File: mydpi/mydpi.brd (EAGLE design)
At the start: 40 x 20 mm, 33 parts, among them U1 MEGA32U4-MU, U2 AP7381-33Y-13, Y1 830069392

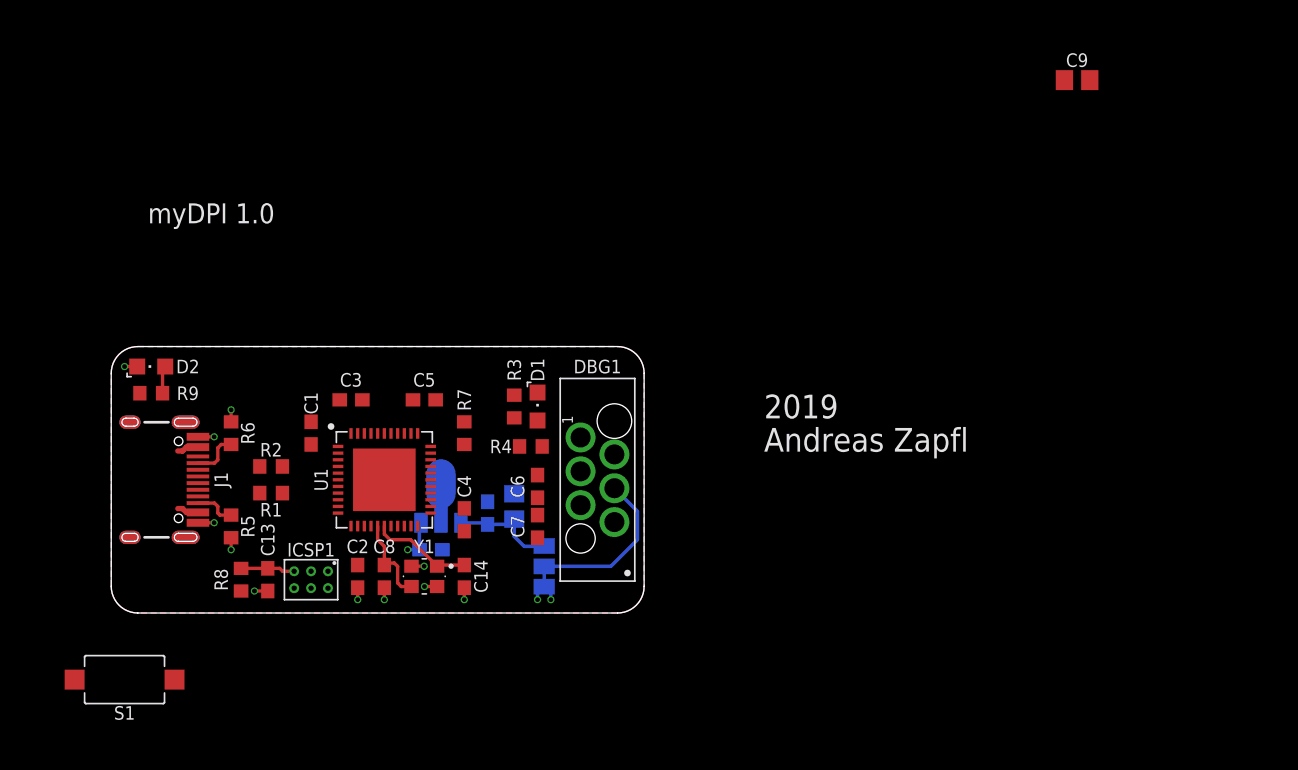
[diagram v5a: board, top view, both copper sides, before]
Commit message: Button and Fuse added
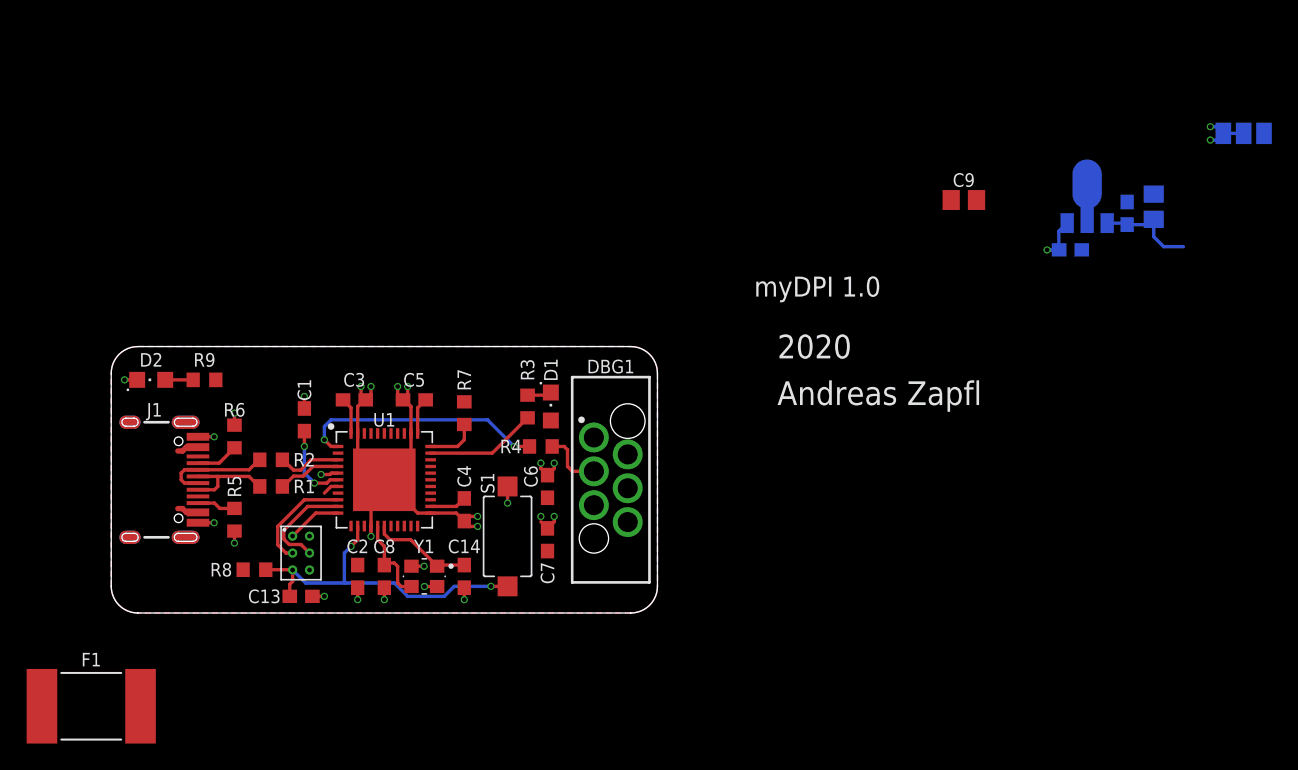
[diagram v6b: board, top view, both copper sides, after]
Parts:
- added F1: 0ZCF0050FF2C, zaan-Fuses:7555
- DBG1: value AVR-UPDI-SKEDD -> AVR-UPDI-6-SKEDD; device zaan-Connectors:490107670612 -> zaan-Connectors:490107670612_DEBUGGING
- moved SJ1 61.7 mm to (85.0, 36.0), turned to 0 degrees
- moved U2 53.5 mm to (73.2, 31.2)
- moved C10 53.0 mm to (78.2, 30.5)
- moved C11 53.0 mm to (76.2, 30.0)
- moved C12 53.0 mm to (72.0, 27.2)
- moved S1 30.7 mm to (29.8, 5.75), turned to 270 degrees
- moved C9 12.4 mm to (64.0, 31.0)
- moved R9 4.12 mm to (7.00, 17.5), turned to 180 degrees
- moved C13 2.80 mm to (14.2, 1.25), turned to 0 degrees
- moved ICSP1 2.14 mm to (14.2, 4.50), turned to 0 degrees
- moved R7 1.50 mm to (26.5, 15.0)
- moved C7 1.25 mm to (32.8, 5.50)
- moved R8 1.25 mm to (10.8, 3.25), turned to 180 degrees
- moved C1 1.12 mm to (14.5, 14.5)
- moved D1 1.00 mm to (33.0, 15.5)
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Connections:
- net GND: now also S1.1
- net RST: now also S1.2
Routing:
- net GND: track 10.8 -> 42.8 mm, vias 11 -> 25
- net RST: track 4.07 -> 26.0 mm, vias 0 -> 2
- net PE6: track 0.00 -> 18.7 mm, vias 0 -> 2
- net MEDBG_VTG: track 12.4 -> 0.00 mm
- net +5V: track 8.60 -> 18.4 mm
- net N$1: track 0.00 -> 8.37 mm
- net USB_N: track 0.00 -> 8.21 mm
- net SCK: track 0.00 -> 8.11 mm
- net PDI: track 0.00 -> 7.84 mm
- net USB_P: track 0.00 -> 7.32 mm
- net N$8: track 0.00 -> 6.09 mm, vias 0 -> 2
- net D_N: track 0.00 -> 4.76 mm
- net D_P: track 0.00 -> 4.74 mm
- net MEDBG_UPDI: track 0.00 -> 4.63 mm
- net PDO: track 0.00 -> 4.13 mm
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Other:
- board size 40 x 20 mm -> 41 x 20 mm
- board text added: "2020"
- board text removed: "2019"

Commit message: LDO added
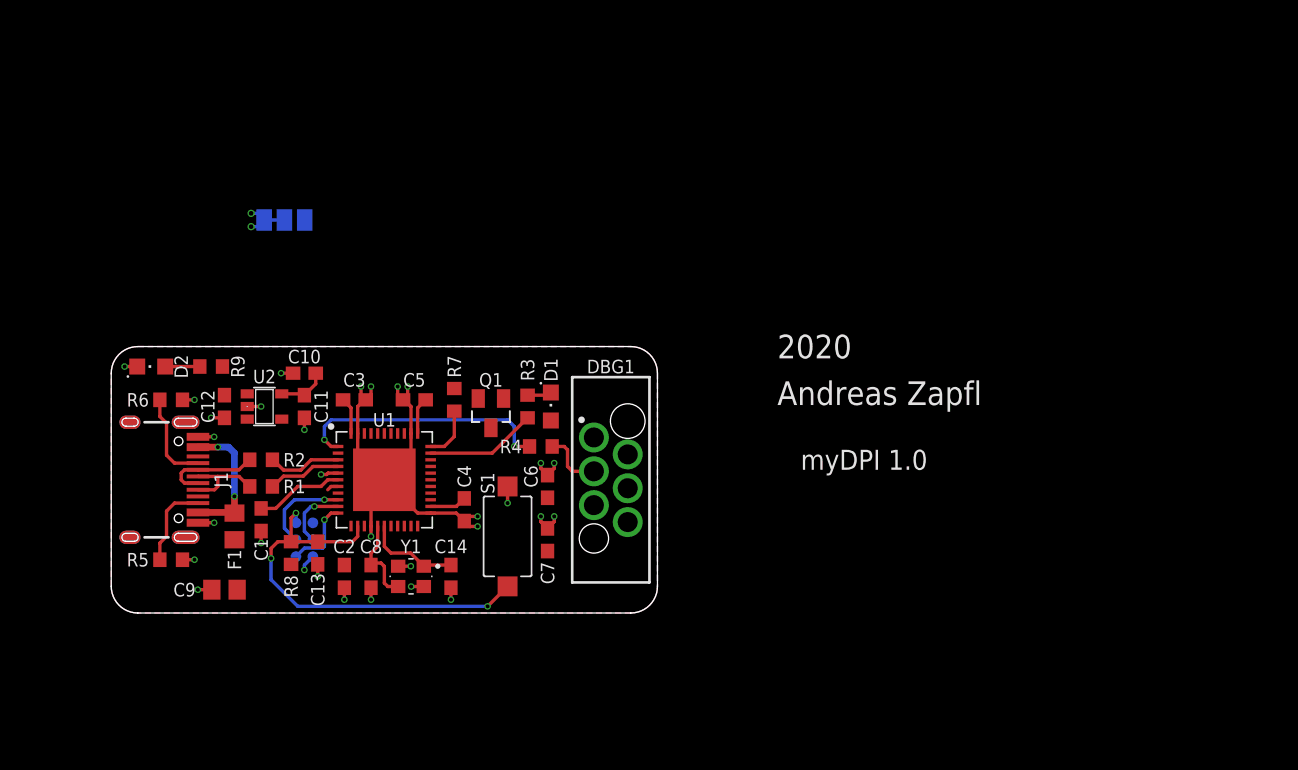
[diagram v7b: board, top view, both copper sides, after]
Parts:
- added Q1: DMN3404L, zaan-Discrete:SOT23
- C10: value 22u -> 1u; device zaan-Capacitors:C0805 -> zaan-Capacitors:C0603
- C12: value 100n -> 1u
- F1: value 0ZCF0050FF2C -> MF-PSMF035X-2; device zaan-Fuses:7555 -> zaan-Fuses:F0805
- ICSP1: value AVR-ISP-1.27MM -> AVR-ISP-SMD; device zaan-Connectors:AVRISP-1.27 -> zaan-Connectors:AVRISP-1.27-SMD
- U2: value AP7381-33Y-13 -> RT9193-33GB; device zaan-IC-Power:SOT89 -> zaan-IC-Power:SOT23-5
- moved SJ1 72.3 mm to (13.0, 29.5)
- moved C10 65.0 mm to (14.5, 18.0), flipped to the top, turned to 180 degrees
- moved C12 64.6 mm to (8.50, 15.5), flipped to the top, turned to 270 degrees
- moved U2 63.7 mm to (11.5, 15.5), flipped to the top, turned to 270 degrees
- moved C11 63.4 mm to (14.5, 15.5), flipped to the top, turned to 270 degrees
- moved C9 62.7 mm to (8.50, 1.75), turned to 180 degrees
- moved F1 17.3 mm to (9.25, 6.50), turned to 270 degrees
- moved C1 8.17 mm to (11.2, 7.00), turned to 270 degrees
- moved R5 5.62 mm to (4.50, 4.00), turned to 180 degrees
- moved R6 5.49 mm to (4.50, 16.0), turned to 180 degrees
- moved C13 3.48 mm to (15.5, 4.50), turned to 270 degrees
- moved R8 3.02 mm to (13.5, 4.50), turned to 270 degrees
- moved R7 1.25 mm to (25.8, 16.0)
- moved R9 1.12 mm to (7.50, 18.5)
- moved ICSP1 1.03 mm to (14.5, 5.50), flipped to the bottom, turned to 180 degrees
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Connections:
- new net N$10: Q1.3
- new net N$11: Q1.2
- new net N$12: F1.1, J1.VBUS1, J1.VBUS2
- new net N$4: Q1.1
- net +3V3: now also U2.5; no longer U2.1
- net +5V: now also C9.1, F1.2, U2.1; no longer J1.VBUS1, J1.VBUS2, U2.3
- net GND: now also C9.2; no longer U2.2@1
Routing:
- net N$12: track 0.00 -> 10.2 mm, vias 0 -> 2
- net RST: track 26.0 -> 32.2 mm, vias 2 -> 3
- net +5V: track 18.4 -> 12.8 mm
- net GND: track 42.8 -> 48.2 mm, vias 25 -> 30
- net +3V3: track 7.55 -> 3.74 mm
- net N$6: track 3.22 -> 6.97 mm
- net N$5: track 2.91 -> 6.47 mm
- net PDI: track 7.84 -> 5.00 mm, vias 0 -> 1
- net PDO: track 4.13 -> 5.69 mm, vias 0 -> 1
- net SCK: track 8.11 -> 6.94 mm, vias 0 -> 1
- net PE6: track 18.7 -> 19.5 mm
- net USB_P: track 7.32 -> 6.57 mm
- net USB_N: track 8.21 -> 7.46 mm
- net D_P: track 4.74 -> 5.49 mm
- net D_N: track 4.76 -> 5.51 mm
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
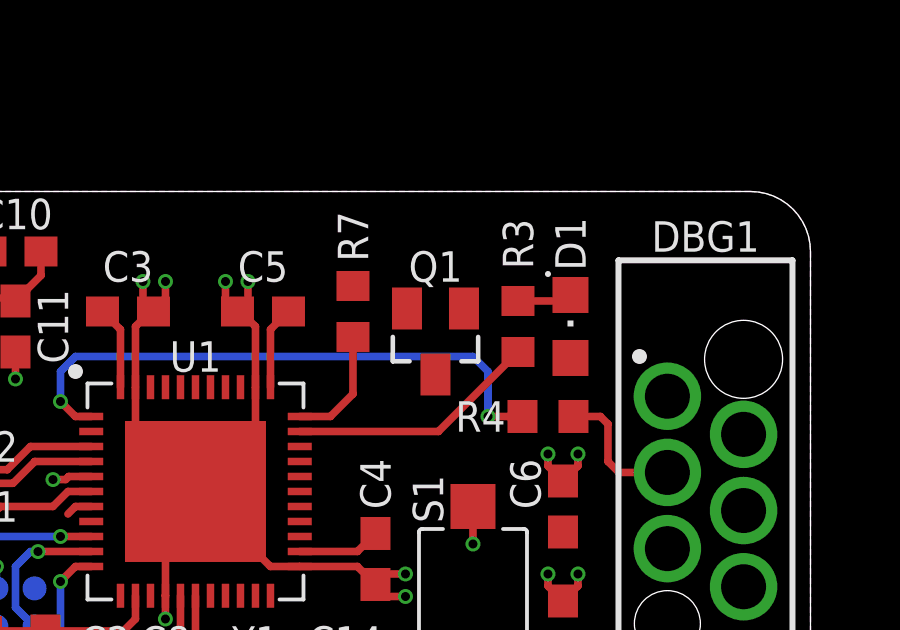
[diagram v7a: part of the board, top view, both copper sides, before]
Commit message: Minor placement change
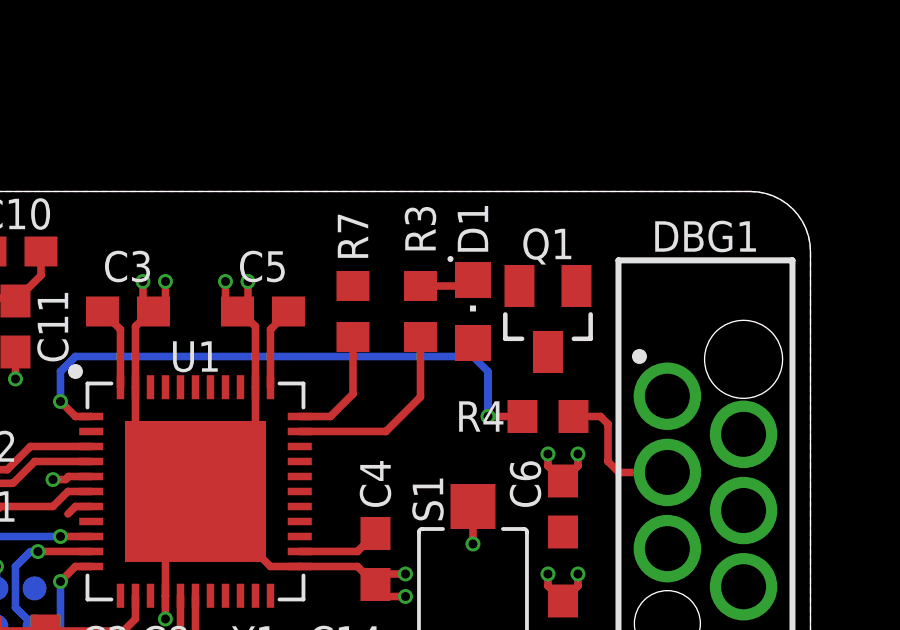
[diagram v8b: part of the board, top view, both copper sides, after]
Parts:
- moved Q1 3.82 mm to (32.2, 15.8)
- moved D1 3.29 mm to (29.8, 16.0)
- moved R3 3.29 mm to (28.0, 16.0)
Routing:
- net N$1: track 8.37 -> 6.50 mm
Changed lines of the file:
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@@
 </layers>
 <board>
-<fusionsync huburn="a.YnVzaW5lc3M6bXllZHUyNzUw" projecturn="a.YnVzaW5lc3M6bXllZHUyNzUwI0QyMDIwMDEyNDI1ODYxMzcwNg" f3durn="urn:adsk.wipprod:dm.lineage:2NjS6xJrTEy7JGCJS98lKg" pcbguid="408126e5-ce63-4758-9e65-038a09f0ee83" lastpulledtime="" lastsyncedchangeguid="23e4f944-fca3-98ec-f6a2-66d46de459b9"/>
+<fusionsync huburn="a.YnVzaW5lc3M6bXllZHUyNzUw" projecturn="a.YnVzaW5lc3M6bXllZHUyNzUwI0QyMDIwMDEyNDI1ODYxMzcwNg" f3durn="urn:adsk.wipprod:dm.lineage:2NjS6xJrTEy7JGCJS98lKg" pcbguid="408126e5-ce63-4758-9e65-038a09f0ee83" lastpulledtime="" lastsyncedchangeguid="fe539757-93f1-18ac-ba5c-e9a8d551b2ab"/>
 <plain>
 <wire x1="0" y1="18" x2="0" y2="2" width="0" layer="20"/>
@@
 <attribute name="VOLTAGE" value="50V" x="32.75" y="5.5" size="1.778" layer="27" rot="R90" display="off"/>
 </element>
-<element name="R3" library="zaan-Resistors" library_urn="urn:adsk.eagle:library:16759442" package="R0603" package3d_urn="urn:adsk.eagle:package:16759452/1" value="1k" x="31.25" y="15.5" smashed="yes" rot="R90">
-<attribute name="DESCRIPTION" value="Surface Mount Resistor" x="31.25" y="15.5" size="1.778" layer="27" rot="R90" display="off"/>
-<attribute name="MF" value="Yageo" x="31.25" y="15.5" size="1.778" layer="27" rot="R90" display="off"/>
-<attribute name="MPN" value="RC0603FR-071KL" x="31.25" y="15.5" size="1.778" layer="27" rot="R90" display="off"/>
-<attribute name="NAME" x="31.25" y="18.25" size="1.016" layer="25" font="vector" ratio="15" rot="R90" align="center"/>
-<attribute name="PACKAGE" value="1608" x="31.25" y="15.5" size="1.778" layer="27" rot="R90" display="off"/>
-<attribute name="PACKAGE-IN" value="0603" x="31.25" y="15.5" size="1.778" layer="27" rot="R90" display="off"/>
-<attribute name="POWER" value="0.1W" x="31.25" y="15.5" size="1.778" layer="27" rot="R90" display="off"/>
-<attribute name="TOLERANCE" value="1%" x="31.25" y="15.5" size="1.778" layer="27" rot="R90" display="off"/>
-<attribute name="VALUE" x="32.75" y="15.5" size="1.016" layer="27" font="vector" ratio="15" rot="R90" align="center"/>
-<attribute name="VOLTAGE" value="75V" x="31.25" y="15.5" size="1.778" layer="27" rot="R90" display="off"/>
-</element>
-<element name="D1" library="zaan-Optoelectronics" library_urn="urn:adsk.eagle:library:16759395" package="CHIPLED_0805" package3d_urn="urn:adsk.eagle:package:16759426/3" value="LTST-C171KSKT" x="33" y="15.5" smashed="yes">
-<attribute name="DESCRIPTION" value="Surface Mount LED" x="33" y="15.5" size="1.778" layer="27" display="off"/>
-<attribute name="MF" value="Lite-On" x="33" y="15.5" size="1.778" layer="27" display="off"/>
-<attribute name="MPN" value="LTST-C171KSKT" x="33" y="15.5" size="1.778" layer="27" display="off"/>
-<attribute name="NAME" x="33" y="18.25" size="1.016" layer="25" font="vector" ratio="15" rot="R90" align="center"/>
-<attribute name="PACKAGE" value="2012" x="33" y="15.5" size="1.778" layer="27" display="off"/>
-<attribute name="PACKAGE-IN" value="0805" x="33" y="15.5" size="1.778" layer="27" display="off"/>
-<attribute name="VALUE" x="34.5" y="15.5" size="1.016" layer="27" font="vector" ratio="15" rot="R90" align="center"/>
+<element name="R3" library="zaan-Resistors" library_urn="urn:adsk.eagle:library:16759442" package="R0603" package3d_urn="urn:adsk.eagle:package:16759452/1" value="1k" x="28" y="16" smashed="yes" rot="R90">
+<attribute name="DESCRIPTION" value="Surface Mount Resistor" x="28" y="16" size="1.778" layer="27" rot="R90" display="off"/>
+<attribute name="MF" value="Yageo" x="28" y="16" size="1.778" layer="27" rot="R90" display="off"/>
+<attribute name="MPN" value="RC0603FR-071KL" x="28" y="16" size="1.778" layer="27" rot="R90" display="off"/>
+<attribute name="NAME" x="28" y="18.75" size="1.016" layer="25" font="vector" ratio="15" rot="R90" align="center"/>
+<attribute name="PACKAGE" value="1608" x="28" y="16" size="1.778" layer="27" rot="R90" display="off"/>
+<attribute name="PACKAGE-IN" value="0603" x="28" y="16" size="1.778" layer="27" rot="R90" display="off"/>
+<attribute name="POWER" value="0.1W" x="28" y="16" size="1.778" layer="27" rot="R90" display="off"/>
+<attribute name="TOLERANCE" value="1%" x="28" y="16" size="1.778" layer="27" rot="R90" display="off"/>
+<attribute name="VALUE" x="29.5" y="16" size="1.016" layer="27" font="vector" ratio="15" rot="R90" align="center"/>
+<attribute name="VOLTAGE" value="75V" x="28" y="16" size="1.778" layer="27" rot="R90" display="off"/>
+</element>
+<element name="D1" library="zaan-Optoelectronics" library_urn="urn:adsk.eagle:library:16759395" package="CHIPLED_0805" package3d_urn="urn:adsk.eagle:package:16759426/3" value="LTST-C171KSKT" x="29.75" y="16" smashed="yes">
+<attribute name="DESCRIPTION" value="Surface Mount LED" x="29.75" y="16" size="1.778" layer="27" display="off"/>
+<attribute name="MF" value="Lite-On" x="29.75" y="16" size="1.778" layer="27" display="off"/>
+<attribute name="MPN" value="LTST-C171KSKT" x="29.75" y="16" size="1.778" layer="27" display="off"/>
+<attribute name="NAME" x="29.75" y="18.75" size="1.016" layer="25" font="vector" ratio="15" rot="R90" align="center"/>
+<attribute name="PACKAGE" value="2012" x="29.75" y="16" size="1.778" layer="27" display="off"/>
+<attribute name="PACKAGE-IN" value="0805" x="29.75" y="16" size="1.778" layer="27" display="off"/>
+<attribute name="VALUE" x="31.25" y="16" size="1.016" layer="27" font="vector" ratio="15" rot="R90" align="center"/>
 </element>
 <element name="J1" library="zaan-Connectors" library_urn="urn:adsk.eagle:library:16759010" package="USB-C-16P" package3d_urn="urn:adsk.eagle:package:16672513/2" value="" x="2.5" y="10" smashed="yes" rot="R270">
@@
 <attribute name="VALUE" x="9" y="15.5" size="1.016" layer="27" font="vector" ratio="15" rot="R270" align="center"/>
 </element>
-<element name="Q1" library="zaan-Discrete" library_urn="urn:adsk.eagle:library:16759095" package="SOT23" package3d_urn="urn:adsk.eagle:package:16759132/1" value="DMN3404L" x="28.5" y="15" smashed="yes" rot="R180">
-<attribute name="DESCRIPTION" value="N-CHANNEL MOSFET" x="28.5" y="15" size="1.778" layer="27" rot="R180" display="off"/>
-<attribute name="MF" value="Diodes Incorporated" x="28.5" y="15" size="1.778" layer="27" rot="R180" display="off"/>
-<attribute name="MPN" value="DMN3404L-7" x="28.5" y="15" size="1.778" layer="27" rot="R180" display="off"/>
-<attribute name="NAME" x="28.5" y="17.5" size="1.016" layer="25" font="vector" ratio="15" rot="R180" align="center"/>
-<attribute name="PACKAGE" value="SOT-23" x="28.5" y="15" size="1.778" layer="27" rot="R180" display="off"/>
-<attribute name="VALUE" x="28.5" y="17.5" size="1.016" layer="27" font="vector" ratio="15" rot="R180" align="center"/>
+<element name="Q1" library="zaan-Discrete" library_urn="urn:adsk.eagle:library:16759095" package="SOT23" package3d_urn="urn:adsk.eagle:package:16759132/1" value="DMN3404L" x="32.25" y="15.75" smashed="yes" rot="R180">
+<attribute name="DESCRIPTION" value="N-CHANNEL MOSFET" x="32.25" y="15.75" size="1.778" layer="27" rot="R180" display="off"/>
+<attribute name="MF" value="Diodes Incorporated" x="32.25" y="15.75" size="1.778" layer="27" rot="R180" display="off"/>
+<attribute name="MPN" value="DMN3404L-7" x="32.25" y="15.75" size="1.778" layer="27" rot="R180" display="off"/>
+<attribute name="NAME" x="32.25" y="18.25" size="1.016" layer="25" font="vector" ratio="15" rot="R180" align="center"/>
+<attribute name="PACKAGE" value="SOT-23" x="32.25" y="15.75" size="1.778" layer="27" rot="R180" display="off"/>
+<attribute name="VALUE" x="32.25" y="18.25" size="1.016" layer="27" font="vector" ratio="15" rot="R180" align="center"/>
 </element>
 </elements>
@@
 <contactref element="U1" pad="32"/>
 <contactref element="R3" pad="1"/>
-<wire x1="28.6" y1="12" x2="23.975" y2="12" width="0.254" layer="1"/>
-<wire x1="28.6" y1="12" x2="31.25" y2="14.65" width="0.254" layer="1"/>
+<wire x1="26.85" y1="12" x2="23.975" y2="12" width="0.254" layer="1"/>
+<wire x1="28" y1="13.15" x2="28" y2="15.15" width="0.254" layer="1"/>
+<wire x1="28" y1="13.15" x2="26.85" y2="12" width="0.254" layer="1"/>
 </signal>
 <signal name="N$2">
 <contactref element="R3" pad="2"/>
 <contactref element="D1" pad="C"/>
-<wire x1="31.25" y1="16.35" x2="32.8" y2="16.35" width="0.254" layer="1"/>
-<wire x1="32.8" y1="16.35" x2="33" y2="16.55" width="0.254" layer="1"/>
+<wire x1="28" y1="16.85" x2="29.55" y2="16.85" width="0.254" layer="1"/>
+<wire x1="29.55" y1="16.85" x2="29.75" y2="17.05" width="0.254" layer="1"/>
 </signal>
 <signal name="USB_P" class="1">
